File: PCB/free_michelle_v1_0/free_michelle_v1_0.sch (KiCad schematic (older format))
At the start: 7 parts

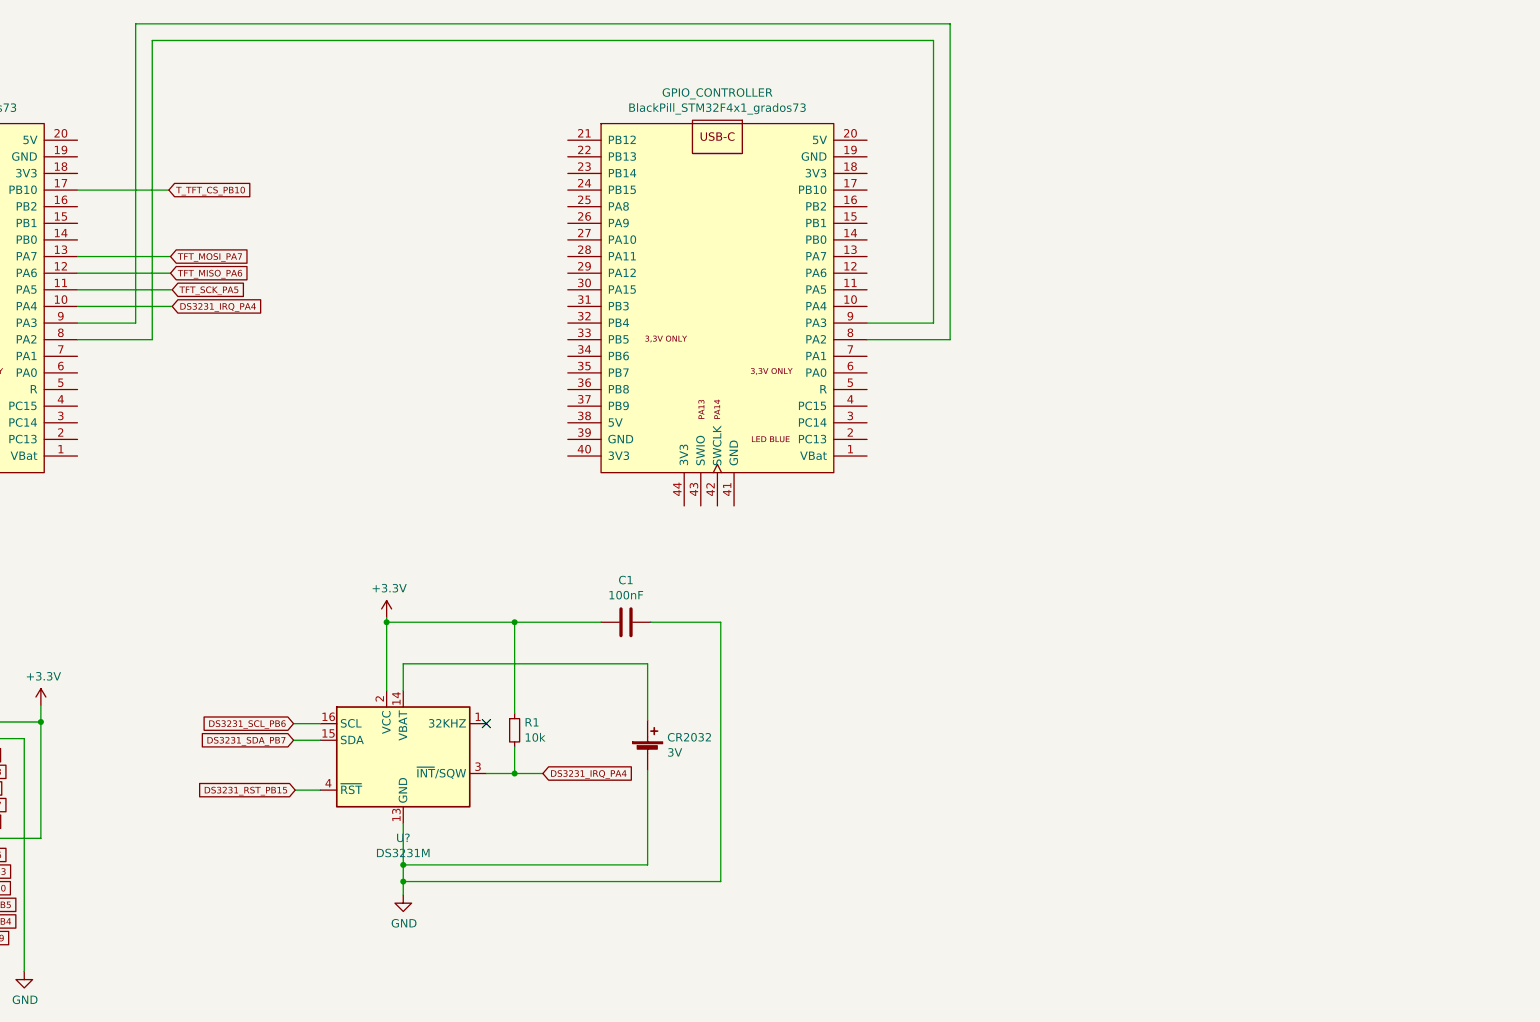
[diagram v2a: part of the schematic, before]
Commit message: Dodane zapomniane rezystory podciągające dla SCL i SDA
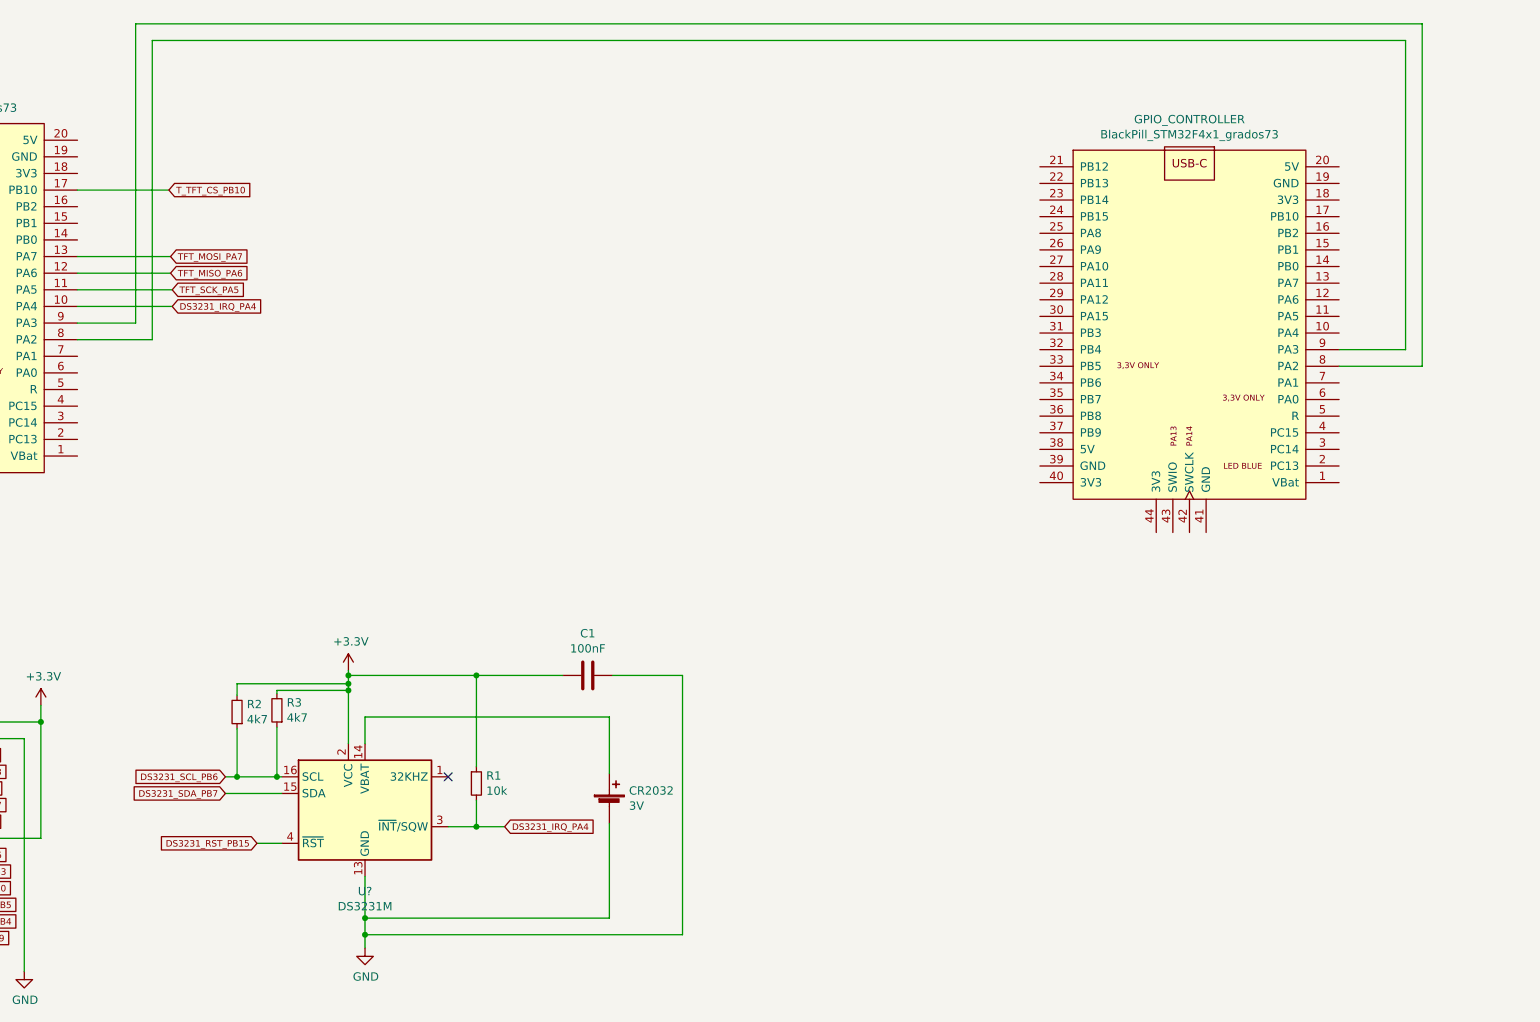
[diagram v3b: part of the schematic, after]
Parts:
- added R2, R3: 4k7, symbol Device:R_Small
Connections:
- net +3V3: now also R2.2, R3.2
- net DS3231_SCL_PB6: now also R2.1, R3.1
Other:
- moved on the sheet: C1, CR2032, GPIO_CONTROLLER, R1, U?
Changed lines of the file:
@@
 L grad73_library:BlackPill_STM32F4x1_grados73 GPIO_CONTROLLER
 U 1 1 61DBA5F5
-P 7400 2500
-F 0 "GPIO_CONTROLLER" H 7400 3685 50  0000 C CNN
-F 1 "BlackPill_STM32F4x1_grados73" H 7400 3594 50  0000 C CNN
-F 2 "" H 8200 1500 50  0001 C CNN
-F 3 "" H 8200 1500 50  0001 C CNN
-	1    7400 2500
+P 10240 2660
+F 0 "GPIO_CONTROLLER" H 10240 3845 50  0000 C CNN
+F 1 "BlackPill_STM32F4x1_grados73" H 10240 3754 50  0000 C CNN
+F 2 "" H 11040 1660 50  0001 C CNN
+F 3 "" H 11040 1660 50  0001 C CNN
+	1    10240 2660
 	1    0    0    -1
 $EndComp
@@
 	4000 2800 4000 1000
 Wire Wire Line
-	4000 1000 8700 1000
-Wire Wire Line
-	8700 1000 8700 2700
-Wire Wire Line
-	8700 2700 8300 2700
+	11540 2860 11140 2860
 Wire Wire Line
 	3550 2700 3900 2700
@@
 	3900 2700 3900 900
 Wire Wire Line
-	3900 900  8800 900
-Wire Wire Line
-	8800 900  8800 2800
-Wire Wire Line
-	8800 2800 8300 2800
+	11640 2960 11140 2960
 $Comp
 L grad73_library:TFT_320x240_ILI9341 D1
@@
 L Timer_RTC:DS3231M U?
 U 1 1 61DE62B5
-P 5510 5310
-F 0 "U?" H 5510 4821 50  0000 C CNN
-F 1 "DS3231M" H 5510 4730 50  0000 C CNN
-F 2 "Package_SO:SOIC-16W_7.5x10.3mm_P1.27mm" H 5510 4710 50  0001 C CNN
-F 3 "http://datasheets.maximintegrated.com/en/ds/DS3231.pdf" H 5780 5360 50  0001 C CNN
-	1    5510 5310
-	1    0    0    -1
-$EndComp
-NoConn ~ 6010 5110
-Text GLabel 4850 5110 0    39   Input ~ 0
+P 5280 5630
+F 0 "U?" H 5280 5141 50  0000 C CNN
+F 1 "DS3231M" H 5280 5050 50  0000 C CNN
+F 2 "Package_SO:SOIC-16W_7.5x10.3mm_P1.27mm" H 5280 5030 50  0001 C CNN
+F 3 "http://datasheets.maximintegrated.com/en/ds/DS3231.pdf" H 5550 5680 50  0001 C CNN
+	1    5280 5630
+	1    0    0    -1
+$EndComp
+NoConn ~ 5780 5430
+Text GLabel 4440 5430 0    39   Input ~ 0
 DS3231_SCL_PB6
 Text GLabel 1600 2900 0    39   Input ~ 0
@@
 Wire Wire Line
 	1600 2900 1750 2900
-Wire Wire Line
-	4850 5110 5010 5110
-Text GLabel 4850 5210 0    39   Input ~ 0
+Text GLabel 4440 5530 0    39   Input ~ 0
 DS3231_SDA_PB7
-Wire Wire Line
-	4850 5210 5010 5210
 Text GLabel 1600 3000 0    39   Input ~ 0
 DS3231_SDA_PB7
@@
 L power:+3.3V #PWR?
 U 1 1 61DEE9A8
-P 5410 4470
-F 0 "#PWR?" H 5410 4320 50  0001 C CNN
-F 1 "+3.3V" H 5425 4643 50  0000 C CNN
-F 2 "" H 5410 4470 50  0001 C CNN
-F 3 "" H 5410 4470 50  0001 C CNN
-	1    5410 4470
+P 5180 4790
+F 0 "#PWR?" H 5180 4640 50  0001 C CNN
+F 1 "+3.3V" H 5195 4963 50  0000 C CNN
+F 2 "" H 5180 4790 50  0001 C CNN
+F 3 "" H 5180 4790 50  0001 C CNN
+	1    5180 4790
 	1    0    0    -1
 $EndComp
@@
 L power:GND #PWR?
 U 1 1 61DF0A08
-P 5510 6140
-F 0 "#PWR?" H 5510 5890 50  0001 C CNN
-F 1 "GND" H 5515 5967 50  0000 C CNN
-F 2 "" H 5510 6140 50  0001 C CNN
-F 3 "" H 5510 6140 50  0001 C CNN
-	1    5510 6140
+P 5280 6460
+F 0 "#PWR?" H 5280 6210 50  0001 C CNN
+F 1 "GND" H 5285 6287 50  0000 C CNN
+F 2 "" H 5280 6460 50  0001 C CNN
+F 3 "" H 5280 6460 50  0001 C CNN
+	1    5280 6460
 	1    0    0    -1
 $EndComp
@@
 L Device:Battery_Cell CR2032
 U 1 1 61DF2F26
-P 6980 5290
-F 0 "CR2032" H 7098 5386 50  0000 L CNN
-F 1 "3V" H 7098 5295 50  0000 L CNN
-F 2 "" V 6980 5350 50  0001 C CNN
-F 3 "~" V 6980 5350 50  0001 C CNN
-	1    6980 5290
-	1    0    0    -1
-$EndComp
-Wire Wire Line
-	6980 5090 6980 4750
-Wire Wire Line
-	6980 4750 5510 4750
-Wire Wire Line
-	5510 4750 5510 4910
-Wire Wire Line
-	6980 5390 6980 5960
-Wire Wire Line
-	6980 5960 5510 5960
-Connection ~ 5510 5960
-Wire Wire Line
-	5510 5960 5510 5710
-Text GLabel 6350 5410 2    39   Input ~ 0
+P 6750 5610
+F 0 "CR2032" H 6868 5706 50  0000 L CNN
+F 1 "3V" H 6868 5615 50  0000 L CNN
+F 2 "" V 6750 5670 50  0001 C CNN
+F 3 "~" V 6750 5670 50  0001 C CNN
+	1    6750 5610
+	1    0    0    -1
+$EndComp
+Wire Wire Line
+	6750 5410 6750 5070
+Wire Wire Line
+	6750 5070 5280 5070
+Wire Wire Line
+	5280 5070 5280 5230
+Wire Wire Line
+	6750 5710 6750 6280
+Wire Wire Line
+	6750 6280 5280 6280
+Connection ~ 5280 6280
+Wire Wire Line
+	5280 6280 5280 6030
+Text GLabel 6120 5730 2    39   Input ~ 0
 DS3231_IRQ_PA4
 Wire Wire Line
-	6010 5410 6180 5410
-Wire Wire Line
-	5410 4470 5410 4500
+	5780 5730 5950 5730
+Wire Wire Line
+	5180 4790 5180 4820
 $Comp
 L Device:R_Small R1
 U 1 1 61DFE4B3
-P 6180 5150
-F 0 "R1" H 6239 5196 50  0000 L CNN
-F 1 "10k" H 6239 5105 50  0000 L CNN
-F 2 "" H 6180 5150 50  0001 C CNN
-F 3 "~" H 6180 5150 50  0001 C CNN
-	1    6180 5150
-	1    0    0    -1
-$EndComp
-Wire Wire Line
-	6180 5250 6180 5410
-Connection ~ 6180 5410
-Wire Wire Line
-	6180 5410 6350 5410
-Wire Wire Line
-	6180 5050 6180 4500
-Wire Wire Line
-	6180 4500 5410 4500
-Connection ~ 5410 4500
-Wire Wire Line
-	5410 4500 5410 4910
-Wire Wire Line
-	5510 5960 5510 6060
-Wire Wire Line
-	7420 4500 7420 6060
-Wire Wire Line
-	7420 6060 5510 6060
-Connection ~ 5510 6060
-Wire Wire Line
-	5510 6060 5510 6140
+P 5950 5470
+F 0 "R1" H 6009 5516 50  0000 L CNN
+F 1 "10k" H 6009 5425 50  0000 L CNN
+F 2 "" H 5950 5470 50  0001 C CNN
+F 3 "~" H 5950 5470 50  0001 C CNN
+	1    5950 5470
+	1    0    0    -1
+$EndComp
+Wire Wire Line
+	5950 5570 5950 5730
+Connection ~ 5950 5730
+Wire Wire Line
+	5950 5730 6120 5730
+Wire Wire Line
+	5950 5370 5950 4820
+Wire Wire Line
+	5950 4820 5180 4820
+Connection ~ 5180 4820
+Wire Wire Line
+	5180 4820 5180 4870
+Wire Wire Line
+	5280 6280 5280 6380
+Wire Wire Line
+	7190 4820 7190 6380
+Wire Wire Line
+	7190 6380 5280 6380
+Connection ~ 5280 6380
+Wire Wire Line
+	5280 6380 5280 6460
 $Comp
 L Device:C C1
 U 1 1 61E06AF8
-P 6850 4500
-F 0 "C1" V 7102 4500 50  0000 C CNN
-F 1 "100nF" V 7011 4500 50  0000 C CNN
-F 2 "" H 6888 4350 50  0001 C CNN
-F 3 "~" H 6850 4500 50  0001 C CNN
-	1    6850 4500
+P 6620 4820
+F 0 "C1" V 6872 4820 50  0000 C CNN
+F 1 "100nF" V 6781 4820 50  0000 C CNN
+F 2 "" H 6658 4670 50  0001 C CNN
+F 3 "~" H 6620 4820 50  0001 C CNN
+	1    6620 4820
 	0    -1   -1   0
 $EndComp
 Wire Wire Line
-	6180 4500 6700 4500
-Connection ~ 6180 4500
-Wire Wire Line
-	7000 4500 7420 4500
-Text GLabel 4860 5510 0    39   Input ~ 0
+	5950 4820 6470 4820
+Connection ~ 5950 4820
+Wire Wire Line
+	6770 4820 7190 4820
+Text GLabel 4630 5830 0    39   Input ~ 0
 DS3231_RST_PB15
 Wire Wire Line
-	4860 5510 5010 5510
+	4630 5830 4780 5830
 Text GLabel 1590 1900 0    39   Input ~ 0
 DS3231_RST_PB15
 Wire Wire Line
 	1590 1900 1750 1900
+Wire Wire Line
+	11640 900  11640 2960
+Wire Wire Line
+	3900 900  11640 900
+Wire Wire Line
+	11540 1000 11540 2860
+Wire Wire Line
+	4000 1000 11540 1000
+$Comp
+L Device:R_Small R2
+U 1 1 61DB60FA
+P 4510 5040
+F 0 "R2" H 4451 4994 50  0000 R CNN
+F 1 "4k7" H 4451 5085 50  0000 R CNN
+F 2 "" H 4510 5040 50  0001 C CNN
+F 3 "~" H 4510 5040 50  0001 C CNN
+	1    4510 5040
+	-1   0    0    1
+$EndComp
+$Comp
+L Device:R_Small R3
+U 1 1 61DC4213
+P 4750 5030
+F 0 "R3" H 4691 4984 50  0000 R CNN
+F 1 "4k7" H 4691 5075 50  0000 R CNN
+F 2 "" H 4750 5030 50  0001 C CNN
+F 3 "~" H 4750 5030 50  0001 C CNN
+	1    4750 5030
+	-1   0    0    1
+$EndComp
+Wire Wire Line
+	4440 5530 4780 5530
+Wire Wire Line
+	4440 5430 4510 5430
+Wire Wire Line
+	4510 5140 4510 5430
+Connection ~ 4510 5430
+Wire Wire Line
+	4510 5430 4750 5430
+Wire Wire Line
+	4510 4940 4510 4870
+Wire Wire Line
+	4510 4870 5180 4870
+Connection ~ 5180 4870
+Wire Wire Line
+	5180 4870 5180 4910
+Wire Wire Line
+	4750 4930 4750 4910
+Wire Wire Line
+	4750 4910 5180 4910
+Connection ~ 5180 4910
+Wire Wire Line
+	5180 4910 5180 5230
+Wire Wire Line
+	4750 5130 4750 5430
+Connection ~ 4750 5430
+Wire Wire Line
+	4750 5430 4780 5430
 $EndSCHEMATC

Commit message: Dodany do schematu element EEPROM 24AA01
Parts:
- added R4, R5: 4K7, symbol Device:R_Small
- added U?: 24AA01, symbol grad73_library:24AA01
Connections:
- net +3V3: now also R4.1, R5.1, U?.8 (VCC)
- net GND: now also U?.4 (VSS), U?.7 (WP)
- net EEPROM_SCL_PA8: now reaches TFT_CONTROLLER.25 (PA8)
- net EEPROM_SCL_PA8: now also R4.2, U?.6 (SCL)
- net EEPROM_SDA_PB8: now reaches TFT_CONTROLLER.36 (PB8)
- net EEPROM_SDA_PB8: now also R5.2, U?.5 (SDA)
- no-connect marks 1 -> 4
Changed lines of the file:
@@
 Wire Wire Line
 	4750 5430 4780 5430
+$Comp
+L grad73_library:24AA01 U?
+U 1 1 61DD6889
+P 2240 7320
+F 0 "U?" H 2265 7435 50  0000 C CNN
+F 1 "24AA01" H 2265 7344 50  0000 C CNN
+F 2 "" H 2240 7320 50  0001 C CNN
+F 3 "" H 2240 7320 50  0001 C CNN
+	1    2240 7320
+	1    0    0    -1
+$EndComp
+$Comp
+L power:GND #PWR?
+U 1 1 61DD74E4
+P 1800 8030
+F 0 "#PWR?" H 1800 7780 50  0001 C CNN
+F 1 "GND" H 1805 7857 50  0000 C CNN
+F 2 "" H 1800 8030 50  0001 C CNN
+F 3 "" H 1800 8030 50  0001 C CNN
+	1    1800 8030
+	1    0    0    -1
+$EndComp
+Wire Wire Line
+	1800 7770 1940 7770
+Wire Wire Line
+	1800 7770 1800 7900
+Wire Wire Line
+	2590 7570 2650 7570
+Wire Wire Line
+	2650 7570 2650 7900
+Wire Wire Line
+	2650 7900 1800 7900
+Connection ~ 1800 7900
+Wire Wire Line
+	1800 7900 1800 8030
+$Comp
+L free_michelle_v1_0-cache:+3.3V #PWR?
+U 1 1 61DBFF7C
+P 2700 7300
+F 0 "#PWR?" H 2700 7150 50  0001 C CNN
+F 1 "+3.3V" H 2715 7473 50  0000 C CNN
+F 2 "" H 2700 7300 50  0001 C CNN
+F 3 "" H 2700 7300 50  0001 C CNN
+	1    2700 7300
+	1    0    0    -1
+$EndComp
+Wire Wire Line
+	2590 7470 2700 7470
+Wire Wire Line
+	2700 7470 2700 7380
+NoConn ~ 1940 7470
+NoConn ~ 1940 7570
+NoConn ~ 1940 7670
+Text GLabel 3480 7770 2    39   Input ~ 0
+EEPROM_SDA_PB8
+Text GLabel 1600 3100 0    39   Input ~ 0
+EEPROM_SDA_PB8
+Wire Wire Line
+	1600 3100 1750 3100
+Text GLabel 3480 7670 2    39   Input ~ 0
+EEPROM_SCL_PA8
+Text GLabel 1590 2000 0    39   Input ~ 0
+EEPROM_SCL_PA8
+Wire Wire Line
+	1590 2000 1750 2000
+Wire Wire Line
+	2590 7670 2800 7670
+Wire Wire Line
+	2590 7770 3090 7770
+$Comp
+L Device:R_Small R4
+U 1 1 61DDD494
+P 2800 7500
+F 0 "R4" H 2859 7546 50  0000 L CNN
+F 1 "4K7" H 2859 7455 50  0000 L CNN
+F 2 "" H 2800 7500 50  0001 C CNN
+F 3 "~" H 2800 7500 50  0001 C CNN
+	1    2800 7500
+	1    0    0    -1
+$EndComp
+$Comp
+L Device:R_Small R5
+U 1 1 61DDDE8B
+P 3090 7500
+F 0 "R5" H 3149 7546 50  0000 L CNN
+F 1 "4K7" H 3149 7455 50  0000 L CNN
+F 2 "" H 3090 7500 50  0001 C CNN
+F 3 "~" H 3090 7500 50  0001 C CNN
+	1    3090 7500
+	1    0    0    -1
+$EndComp
+Wire Wire Line
+	2800 7600 2800 7670
+Connection ~ 2800 7670
+Wire Wire Line
+	2800 7670 3480 7670
+Wire Wire Line
+	3090 7600 3090 7770
+Connection ~ 3090 7770
+Wire Wire Line
+	3090 7770 3480 7770
+Wire Wire Line
+	2800 7400 2800 7380
+Wire Wire Line
+	2800 7380 2700 7380
+Connection ~ 2700 7380
+Wire Wire Line
+	2700 7380 2700 7330
+Wire Wire Line
+	3090 7400 3090 7330
+Wire Wire Line
+	3090 7330 2700 7330
+Connection ~ 2700 7330
+Wire Wire Line
+	2700 7330 2700 7300
 $EndSCHEMATC

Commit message: Dodany L7805
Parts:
- added C?: 47uF, symbol Device:CP_Small
- added C? (x2): 100nF, symbol Device:C_Small
- added U?: L7805, symbol Regulator_Linear:L7805
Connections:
- net +5V: now also C?.1, U?.3 (OUT)
- net GND: now also C?.2, C?.2, C?.2, U?.2 (GND)
- new net +9V: C?.1, C?.1, U?.1 (IN)
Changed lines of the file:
@@
 Wire Wire Line
 	2700 7330 2700 7300
+$Comp
+L power:PWR_FLAG #FLG?
+U 1 1 61DEC757
+P 12520 1060
+F 0 "#FLG?" H 12520 1135 50  0001 C CNN
+F 1 "PWR_FLAG" H 12520 1233 50  0000 C CNN
+F 2 "" H 12520 1060 50  0001 C CNN
+F 3 "~" H 12520 1060 50  0001 C CNN
+	1    12520 1060
+	1    0    0    -1
+$EndComp
+$Comp
+L power:+9V #PWR?
+U 1 1 61DEE2E8
+P 12520 1140
+F 0 "#PWR?" H 12520 990 50  0001 C CNN
+F 1 "+9V" H 12535 1313 50  0000 C CNN
+F 2 "" H 12520 1140 50  0001 C CNN
+F 3 "" H 12520 1140 50  0001 C CNN
+	1    12520 1140
+	-1   0    0    1
+$EndComp
+Wire Wire Line
+	12520 1140 12520 1060
+$Comp
+L Regulator_Linear:L7805 U?
+U 1 1 61DF26E8
+P 13020 1980
+F 0 "U?" H 13020 2222 50  0000 C CNN
+F 1 "L7805" H 13020 2131 50  0000 C CNN
+F 2 "" H 13045 1830 50  0001 L CIN
+F 3 "http://www.st.com/content/ccc/resource/technical/document/datasheet/41/4f/b3/b0/12/d4/47/88/CD00000444.pdf/files/CD00000444.pdf/jcr:content/translations/en.CD00000444.pdf" H 13020 1930 50  0001 C CNN
+	1    13020 1980
+	1    0    0    -1
+$EndComp
+$Comp
+L power:GND #PWR?
+U 1 1 61DF3DFA
+P 13020 2520
+F 0 "#PWR?" H 13020 2270 50  0001 C CNN
+F 1 "GND" H 13025 2347 50  0000 C CNN
+F 2 "" H 13020 2520 50  0001 C CNN
+F 3 "" H 13020 2520 50  0001 C CNN
+	1    13020 2520
+	1    0    0    -1
+$EndComp
+Wire Wire Line
+	13020 2520 13020 2480
+$Comp
+L power:+9V #PWR?
+U 1 1 61DF7AEA
+P 12100 1810
+F 0 "#PWR?" H 12100 1660 50  0001 C CNN
+F 1 "+9V" H 12115 1983 50  0000 C CNN
+F 2 "" H 12100 1810 50  0001 C CNN
+F 3 "" H 12100 1810 50  0001 C CNN
+	1    12100 1810
+	1    0    0    -1
+$EndComp
+Wire Wire Line
+	12100 1810 12100 1980
+$Comp
+L power:+5V #PWR?
+U 1 1 61DFBCEF
+P 13870 1810
+F 0 "#PWR?" H 13870 1660 50  0001 C CNN
+F 1 "+5V" H 13885 1983 50  0000 C CNN
+F 2 "" H 13870 1810 50  0001 C CNN
+F 3 "" H 13870 1810 50  0001 C CNN
+	1    13870 1810
+	1    0    0    -1
+$EndComp
+Wire Wire Line
+	13870 1810 13870 1980
+Wire Wire Line
+	13870 1980 13480 1980
+$Comp
+L Device:CP_Small C?
+U 1 1 61E00529
+P 12100 2120
+F 0 "C?" H 12188 2166 50  0000 L CNN
+F 1 "47uF" H 12188 2075 50  0000 L CNN
+F 2 "" H 12100 2120 50  0001 C CNN
+F 3 "~" H 12100 2120 50  0001 C CNN
+	1    12100 2120
+	1    0    0    -1
+$EndComp
+$Comp
+L Device:C_Small C?
+U 1 1 61E02529
+P 12460 2120
+F 0 "C?" H 12552 2166 50  0000 L CNN
+F 1 "100nF" H 12552 2075 50  0000 L CNN
+F 2 "" H 12460 2120 50  0001 C CNN
+F 3 "~" H 12460 2120 50  0001 C CNN
+	1    12460 2120
+	1    0    0    -1
+$EndComp
+Wire Wire Line
+	12100 1980 12460 1980
+Wire Wire Line
+	12100 2020 12100 1980
+Connection ~ 12100 1980
+Wire Wire Line
+	12460 2020 12460 1980
+Connection ~ 12460 1980
+Wire Wire Line
+	12460 1980 12720 1980
+Wire Wire Line
+	12100 2220 12100 2480
+Wire Wire Line
+	12100 2480 13020 2480
+Connection ~ 13020 2480
+Wire Wire Line
+	13020 2480 13020 2420
+Wire Wire Line
+	12460 2220 12460 2420
+Wire Wire Line
+	12460 2420 13020 2420
+Connection ~ 13020 2420
+Wire Wire Line
+	13020 2420 13020 2370
+$Comp
+L Device:C_Small C?
+U 1 1 61E310BD
+P 13480 2120
+F 0 "C?" H 13572 2166 50  0000 L CNN
+F 1 "100nF" H 13572 2075 50  0000 L CNN
+F 2 "" H 13480 2120 50  0001 C CNN
+F 3 "~" H 13480 2120 50  0001 C CNN
+	1    13480 2120
+	1    0    0    -1
+$EndComp
+Wire Wire Line
+	13480 2020 13480 1980
+Connection ~ 13480 1980
+Wire Wire Line
+	13480 1980 13320 1980
+Wire Wire Line
+	13480 2220 13480 2370
+Wire Wire Line
+	13480 2370 13020 2370
+Connection ~ 13020 2370
+Wire Wire Line
+	13020 2370 13020 2280
 $EndSCHEMATC
